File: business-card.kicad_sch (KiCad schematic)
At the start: 19 parts, among them J1 TC2030, U1 NT3H2111W0FHKH

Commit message: Use schematic INFO1 as the source for contact personalization
Drive footprint text and the native QR from CONTACT_* fields, replacing
the project-variable aliases. Read INFO1 defaults in the finalizer and
synchronize the output schematic, PCB, QR, vCard and NFC data.

Document the KiCad QR refresh step and regenerate design previews.
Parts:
- INFO1: CONTACT_COMPANY ${PROJ_CONTACT_COMPANY} -> Your Company; CONTACT_EMAIL ${PROJ_CONTACT_EMAIL} -> you@example.com; CONTACT_NAME ${PROJ_CONTACT_NAME} -> Your Name; CONTACT_PHONE ${PROJ_CONTACT_PHONE} -> +1 202-555-0123; CONTACT_ROLE ${PROJ_CONTACT_ROLE} -> Your Role; CONTACT_WEB ${PROJ_CONTACT_WEB} -> example.com; CONTACT_WEB_QR ${PROJ_CONTACT_WEB_QR} -> https://example.com
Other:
- note added: "Edit INFO1's CONTACT_* fields. Update PCB from Schematic (F8), then save and reopen the PCB to refresh the QR."
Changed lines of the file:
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@@
 		)
 	)
+	(text "Edit INFO1's CONTACT_* fields.\nUpdate PCB from Schematic (F8), then\nsave and reopen the PCB to refresh the QR."
+		(exclude_from_sim no)
+		(at 76.2 168.91 0)
+		(effects
+			(font
+				(size 1.27 1.27)
+			)
+			(justify left top)
+		)
+	)
 	(text "Minimal NFC and LED Circuit"
 		(exclude_from_sim no)
@@
 			)
 		)
-		(property "CONTACT_NAME" "${PROJ_CONTACT_NAME}"
+		(property "CONTACT_NAME" "Your Name"
 			(at 21.59 175.26 0)
 			(show_name no)
@@
 			)
 		)
-		(property "CONTACT_COMPANY" "${PROJ_CONTACT_COMPANY}"
+		(property "CONTACT_COMPANY" "Your Company"
 			(at 21.59 179.07 0)
 			(show_name no)
@@
 			)
 		)
-		(property "CONTACT_ROLE" "${PROJ_CONTACT_ROLE}"
+		(property "CONTACT_ROLE" "Your Role"
 			(at 21.59 182.88 0)
 			(show_name no)
@@
 			)
 		)
-		(property "CONTACT_EMAIL" "${PROJ_CONTACT_EMAIL}"
+		(property "CONTACT_EMAIL" "you@example.com"
 			(at 21.59 187.96 0)
 			(show_name no)
@@
 			)
 		)
-		(property "CONTACT_PHONE" "${PROJ_CONTACT_PHONE}"
+		(property "CONTACT_PHONE" "+1 202-555-0123"
 			(at 21.59 191.77 0)
 			(show_name no)
@@
 			)
 		)
-		(property "CONTACT_WEB" "${PROJ_CONTACT_WEB}"
+		(property "CONTACT_WEB" "example.com"
 			(at 21.59 195.58 0)
 			(show_name no)
@@
 			)
 		)
-		(property "CONTACT_WEB_QR" "${PROJ_CONTACT_WEB_QR}"
+		(property "CONTACT_WEB_QR" "https://example.com"
 			(at 44.45 181.61 0)
 			(hide yes)

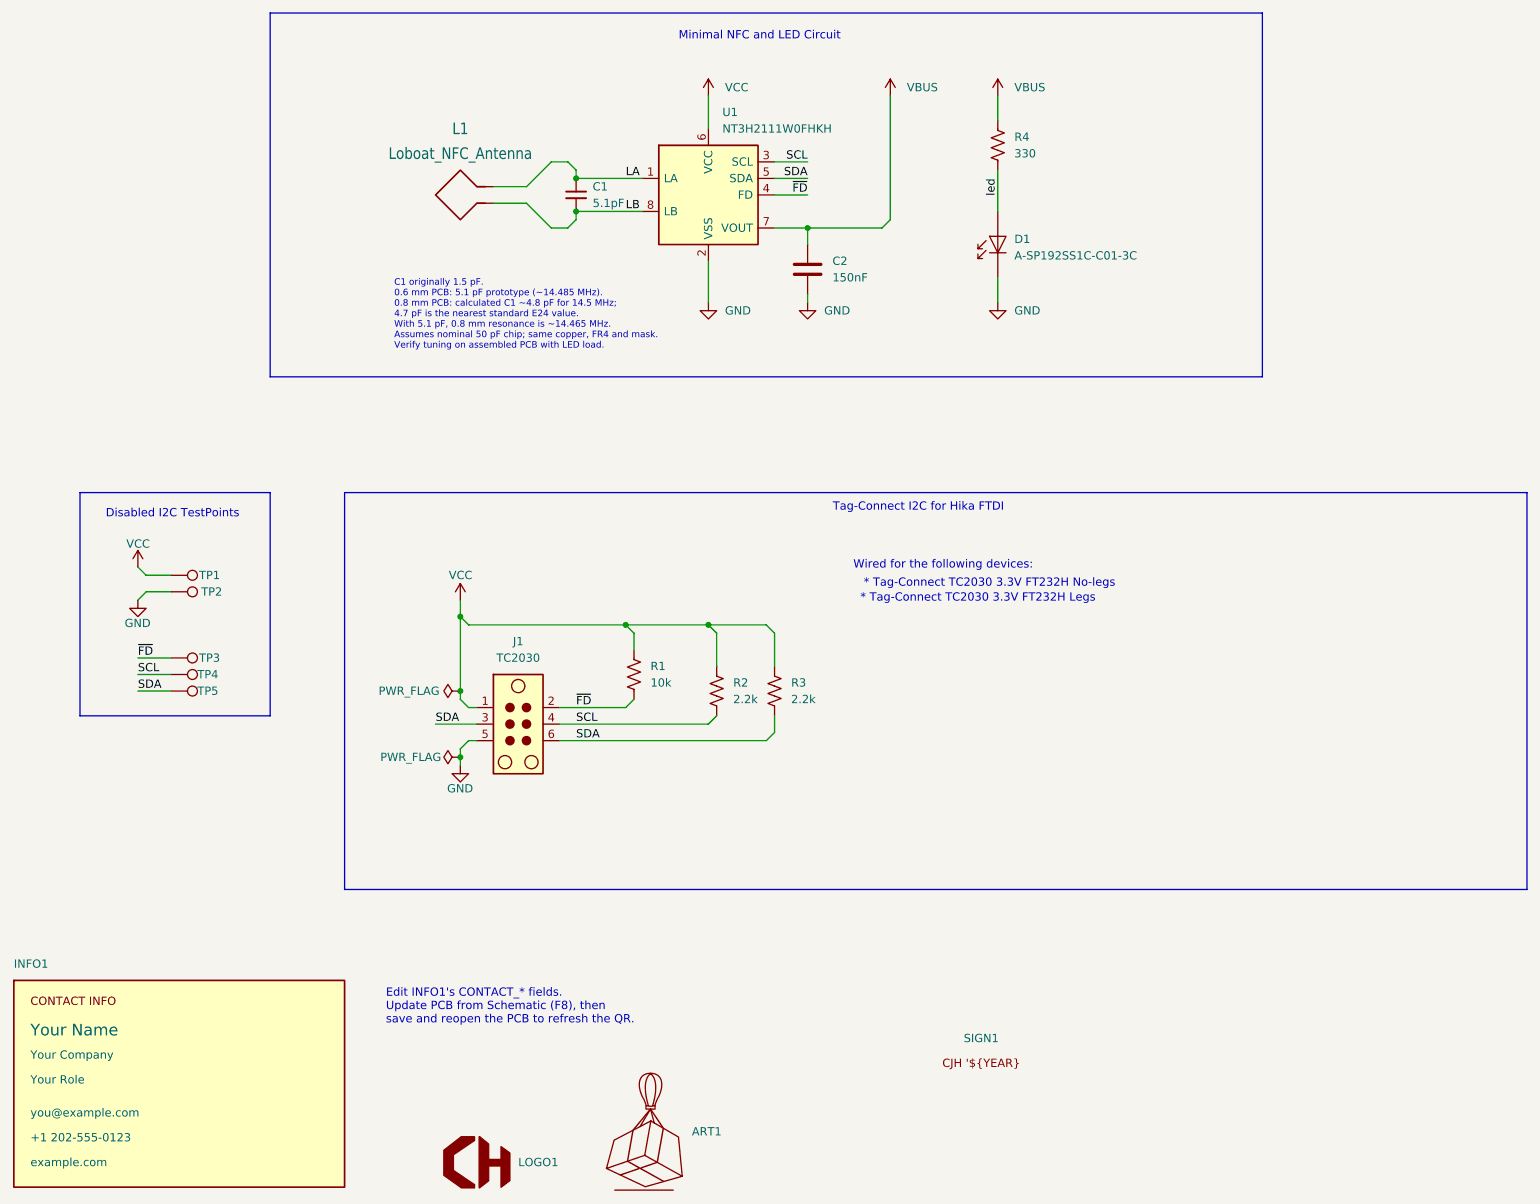
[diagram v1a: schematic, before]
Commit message: Add additional decoupling cap to tag-connect vcc supply
Not the best placement and routing, but this will be
disabled after debugging.
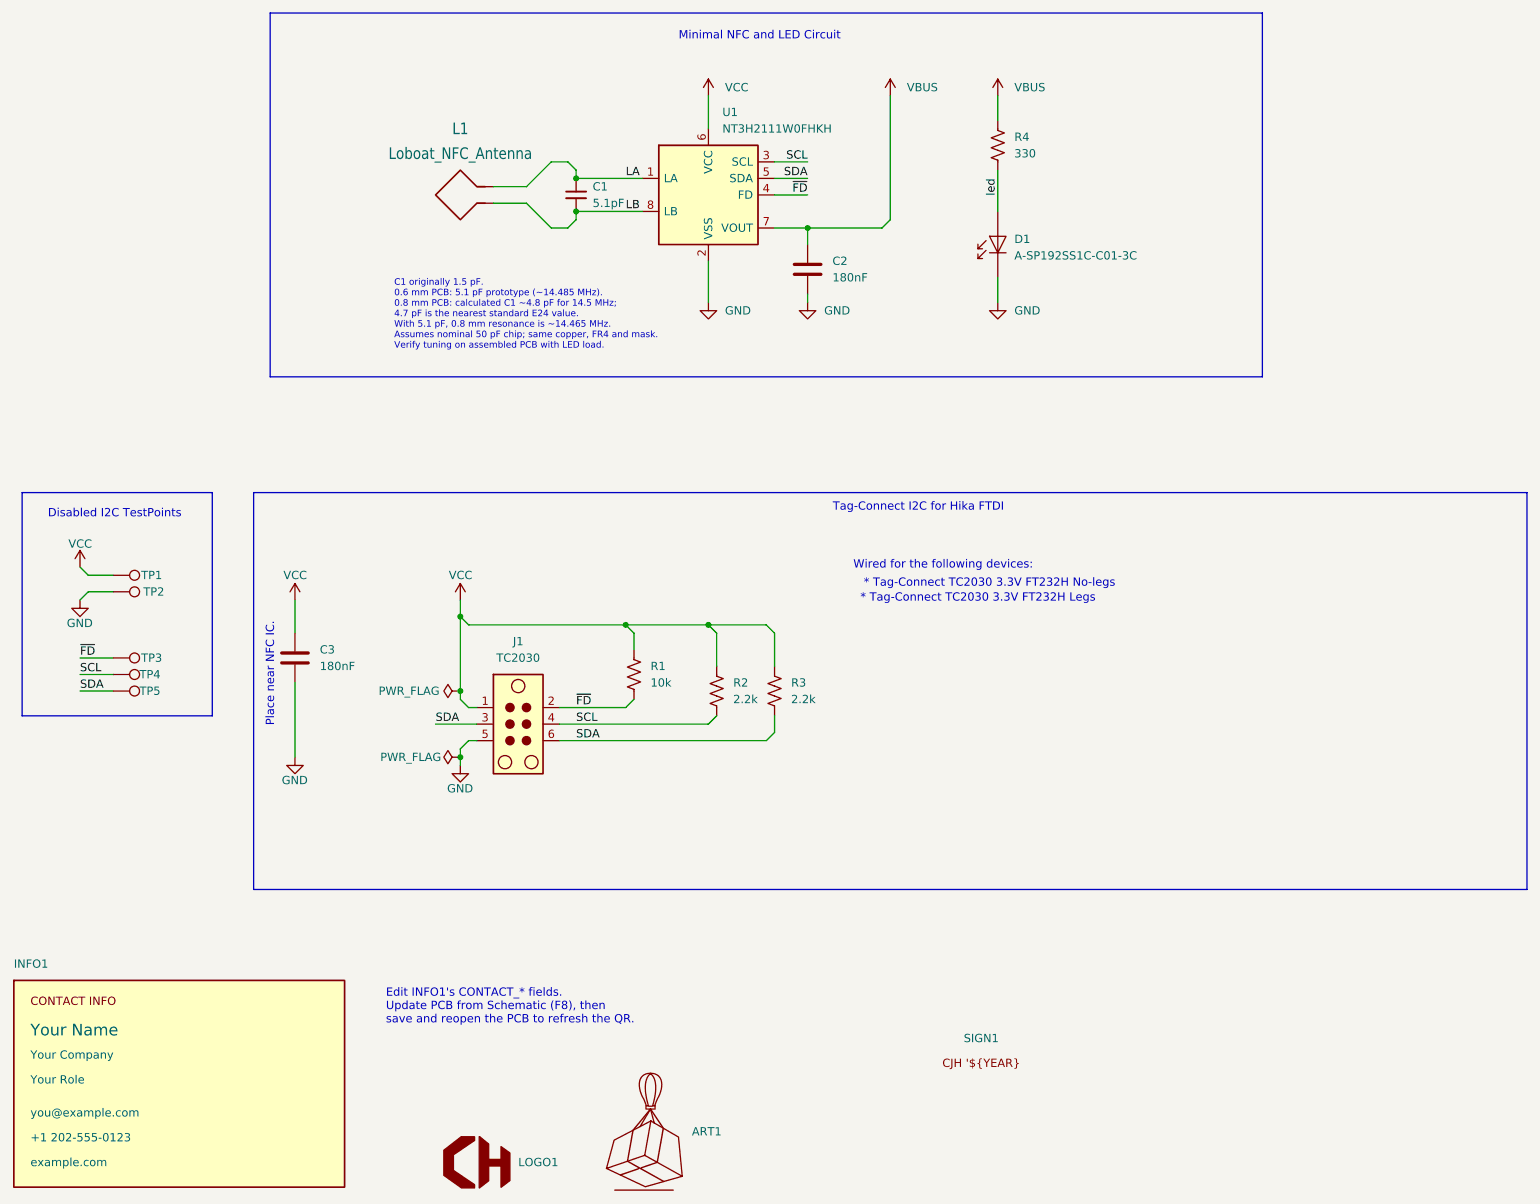
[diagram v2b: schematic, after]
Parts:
- added C3: 180nF, Capacitor_SMD:C_0402_1005Metric_Pad0.74x0.62mm_HandSolder, symbol Device:C
- C2: value 150nF -> 180nF
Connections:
- net GND: now also C3.2
- net VCC: now also C3.1
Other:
- note added: "Place near NFC IC."
- moved on the sheet: TP1, TP2, TP3, TP4, TP5
